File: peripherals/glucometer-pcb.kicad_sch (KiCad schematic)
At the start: 14 parts, among them U1 ESP32_DevKit_V1_DOIT

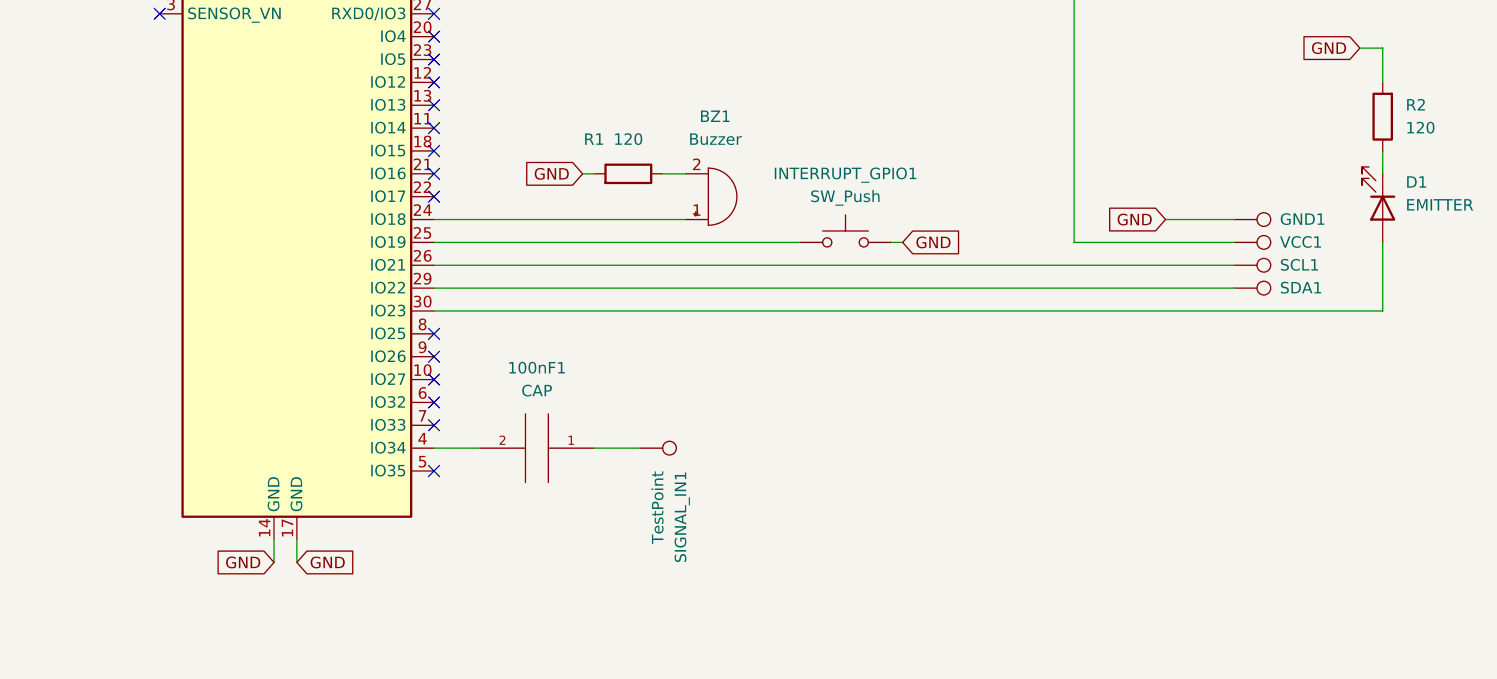
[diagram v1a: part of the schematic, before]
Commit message: updated pcb pads
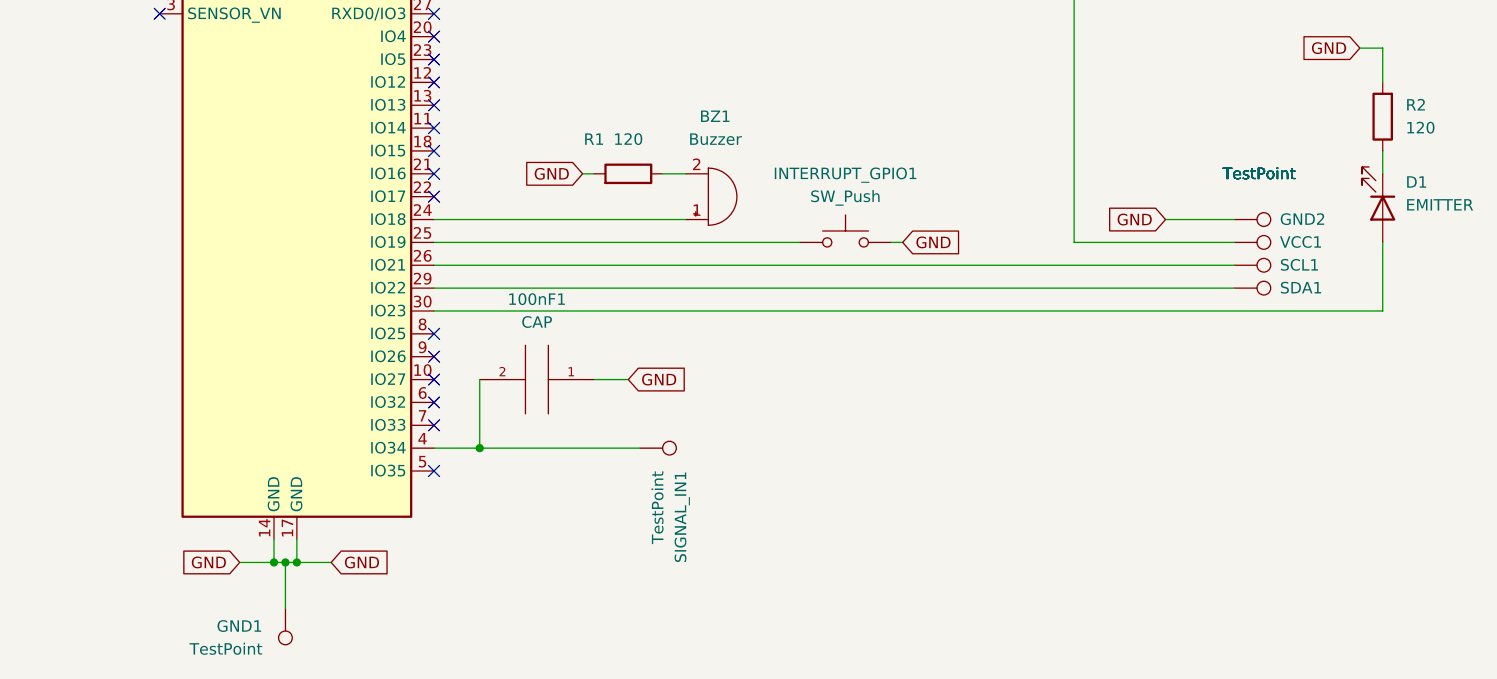
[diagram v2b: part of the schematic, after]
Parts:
- added GND1: TestPoint, TestPoint:TestPoint_Keystone_5015_Micro-Minature, symbol Connector:TestPoint
- GND2: renamed from GND1; value (none) -> TestPoint; footprint (none) -> TestPoint:TestPoint_Pad_2.0x2.0mm
- SCL1, SDA1, VCC1: value (none) -> TestPoint; footprint (none) -> TestPoint:TestPoint_Pad_2.0x2.0mm
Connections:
- net GND: now also 100nF1.1, GND1.1
- net at SIGNAL_IN1.1: now also 100nF1.2, U1.4 (IO34); no longer 100nF1.1
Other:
- moved on the sheet: 100nF1
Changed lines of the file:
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@@
 (kicad_sch (version 20211123) (generator eeschema)
   (paper "A4")
+  (junction (at 67.31 129.54) (diameter 0) (color 0 0 0 0)
+  )
+  (junction (at 66.04 129.54) (diameter 0) (color 0 0 0 0)
+  )
+  (junction (at 88.9 116.84) (diameter 0) (color 0 0 0 0)
+  )
   (junction (at 68.58 48.26) (diameter 0) (color 0 0 0 0)
+  )
+  (junction (at 68.58 129.54) (diameter 0) (color 0 0 0 0)
   )
   (no_connect (at 83.82 106.68))
@@
   (no_connect (at 83.82 114.3))
   (no_connect (at 83.82 86.36))
+  (wire (pts (xy 67.31 134.62) (xy 67.31 129.54))
+    (stroke (width 0) (type default) (color 0 0 0 0))
+  )
+  (wire (pts (xy 88.9 109.22) (xy 88.9 116.84))
+    (stroke (width 0) (type default) (color 0 0 0 0))
+  )
+  (wire (pts (xy 88.9 116.84) (xy 106.68 116.84))
+    (stroke (width 0) (type default) (color 0 0 0 0))
+  )
   (wire (pts (xy 83.82 101.6) (xy 189.23 101.6))
     (stroke (width 0) (type default) (color 0 0 0 0))
@@
     (stroke (width 0) (type default) (color 0 0 0 0))
   )
+  (wire (pts (xy 68.58 129.54) (xy 68.58 127))
+    (stroke (width 0) (type default) (color 0 0 0 0))
+  )
   (wire (pts (xy 83.82 99.06) (xy 172.72 99.06))
     (stroke (width 0) (type default) (color 0 0 0 0))
@@
     (stroke (width 0) (type default) (color 0 0 0 0))
   )
+  (wire (pts (xy 66.04 129.54) (xy 67.31 129.54))
+    (stroke (width 0) (type default) (color 0 0 0 0))
+  )
   (wire (pts (xy 154.94 93.98) (xy 154.94 48.26))
     (stroke (width 0) (type default) (color 0 0 0 0))
@@
     (stroke (width 0) (type default) (color 0 0 0 0))
   )
+  (wire (pts (xy 67.31 129.54) (xy 68.58 129.54))
+    (stroke (width 0) (type default) (color 0 0 0 0))
+  )
   (wire (pts (xy 83.82 91.44) (xy 111.76 91.44))
     (stroke (width 0) (type default) (color 0 0 0 0))
   )
-  (wire (pts (xy 101.6 116.84) (xy 106.68 116.84))
-    (stroke (width 0) (type default) (color 0 0 0 0))
-  )
   (wire (pts (xy 83.82 96.52) (xy 172.72 96.52))
     (stroke (width 0) (type default) (color 0 0 0 0))
@@
     (stroke (width 0) (type default) (color 0 0 0 0))
   )
+  (wire (pts (xy 66.04 129.54) (xy 66.04 127))
+    (stroke (width 0) (type default) (color 0 0 0 0))
+  )
+  (wire (pts (xy 101.6 109.22) (xy 105.41 109.22))
+    (stroke (width 0) (type default) (color 0 0 0 0))
+  )
+  (wire (pts (xy 83.82 116.84) (xy 88.9 116.84))
+    (stroke (width 0) (type default) (color 0 0 0 0))
+  )
   (wire (pts (xy 154.94 93.98) (xy 172.72 93.98))
     (stroke (width 0) (type default) (color 0 0 0 0))
   )
-  (wire (pts (xy 66.04 127) (xy 66.04 129.54))
+  (wire (pts (xy 66.04 129.54) (xy 62.23 129.54))
     (stroke (width 0) (type default) (color 0 0 0 0))
   )
@@
     (stroke (width 0) (type default) (color 0 0 0 0))
   )
-  (wire (pts (xy 83.82 116.84) (xy 88.9 116.84))
-    (stroke (width 0) (type default) (color 0 0 0 0))
-  )
   (wire (pts (xy 189.23 83.82) (xy 189.23 86.36))
     (stroke (width 0) (type default) (color 0 0 0 0))
@@
     (stroke (width 0) (type default) (color 0 0 0 0))
   )
-  (wire (pts (xy 68.58 127) (xy 68.58 129.54))
+  (wire (pts (xy 68.58 129.54) (xy 72.39 129.54))
     (stroke (width 0) (type default) (color 0 0 0 0))
   )
@@
     )
   )
-  (global_label "GND" (shape input) (at 68.58 129.54 0) (fields_autoplaced)
+  (global_label "GND" (shape input) (at 72.39 129.54 0) (fields_autoplaced)
     (effects (font (size 1.27 1.27)) (justify left))
-    (property "Referencias entre hojas" "${INTERSHEET_REFS}" (id 0) (at 74.8636 129.4606 0)
+    (property "Referencias entre hojas" "${INTERSHEET_REFS}" (id 0) (at 78.6736 129.4606 0)
       (effects (font (size 1.27 1.27)) (justify left) hide)
     )
@@
     )
   )
-  (global_label "GND" (shape input) (at 66.04 129.54 180) (fields_autoplaced)
+  (global_label "GND" (shape input) (at 62.23 129.54 180) (fields_autoplaced)
     (effects (font (size 1.27 1.27)) (justify right))
-    (property "Referencias entre hojas" "${INTERSHEET_REFS}" (id 0) (at 59.7564 129.4606 0)
+    (property "Referencias entre hojas" "${INTERSHEET_REFS}" (id 0) (at 55.9464 129.4606 0)
       (effects (font (size 1.27 1.27)) (justify right) hide)
     )
@@
     )
   )
+  (global_label "GND" (shape input) (at 105.41 109.22 0) (fields_autoplaced)
+    (effects (font (size 1.27 1.27)) (justify left))
+    (property "Referencias entre hojas" "${INTERSHEET_REFS}" (id 0) (at 111.6936 109.1406 0)
+      (effects (font (size 1.27 1.27)) (justify left) hide)
+    )
+  )
   (global_label "GND" (shape input) (at 135.89 93.98 0) (fields_autoplaced)
     (effects (font (size 1.27 1.27)) (justify left))
@@
     )
   )
+  (symbol (lib_id "Connector:TestPoint") (at 67.31 134.62 0) (mirror x) (unit 1)
+    (in_bom yes) (on_board yes) (fields_autoplaced)
+    (property "Reference" "GND1" (id 0) (at 64.77 136.6519 0)
+      (effects (font (size 1.27 1.27)) (justify right))
+    )
+    (property "Value" "TestPoint" (id 1) (at 64.77 139.1919 0)
+      (effects (font (size 1.27 1.27)) (justify right))
+    )
+    (property "Footprint" "TestPoint:TestPoint_Keystone_5015_Micro-Minature" (id 2) (at 72.39 134.62 0)
+      (effects (font (size 1.27 1.27)) hide)
+    )
+    (property "Datasheet" "~" (id 3) (at 72.39 134.62 0)
+      (effects (font (size 1.27 1.27)) hide)
+    )
+    (pin "1")
+  )
   (symbol (lib_id "Device:R") (at 105.41 86.36 270) (mirror x) (unit 1)
     (in_bom yes) (on_board yes)
@@
     (pin "1")
   )
-  (symbol (lib_id "pspice:CAP") (at 95.25 116.84 270) (unit 1)
-    (in_bom yes) (on_board yes) (fields_autoplaced)
-    (property "Reference" "100nF1" (id 0) (at 95.25 107.95 90))
-    (property "Value" "CAP" (id 1) (at 95.25 110.49 90))
-    (property "Footprint" "Capacitor_THT:C_Disc_D4.3mm_W1.9mm_P5.00mm" (id 2) (at 95.25 116.84 0)
-      (effects (font (size 1.27 1.27)) hide)
-    )
-    (property "Datasheet" "~" (id 3) (at 95.25 116.84 0)
+  (symbol (lib_id "pspice:CAP") (at 95.25 109.22 270) (unit 1)
+    (in_bom yes) (on_board yes) (fields_autoplaced)
+    (property "Reference" "100nF1" (id 0) (at 95.25 100.33 90))
+    (property "Value" "CAP" (id 1) (at 95.25 102.87 90))
+    (property "Footprint" "Capacitor_THT:C_Disc_D4.3mm_W1.9mm_P5.00mm" (id 2) (at 95.25 109.22 0)
+      (effects (font (size 1.27 1.27)) hide)
+    )
+    (property "Datasheet" "~" (id 3) (at 95.25 109.22 0)
       (effects (font (size 1.27 1.27)) hide)
     )
@@
   (symbol (lib_id "Connector:TestPoint") (at 172.72 91.44 270) (mirror x) (unit 1)
     (in_bom yes) (on_board yes)
-    (property "Reference" "GND1" (id 0) (at 177.8 91.44 90)
-      (effects (font (size 1.27 1.27)) (justify left))
-    )
-    (property "Value" "" (id 1) (at 171.45 86.36 90)
-      (effects (font (size 1.27 1.27)) (justify left))
-    )
-    (property "Footprint" "" (id 2) (at 172.72 86.36 0)
+    (property "Reference" "GND2" (id 0) (at 177.8 91.44 90)
+      (effects (font (size 1.27 1.27)) (justify left))
+    )
+    (property "Value" "TestPoint" (id 1) (at 171.45 86.36 90)
+      (effects (font (size 1.27 1.27)) (justify left))
+    )
+    (property "Footprint" "TestPoint:TestPoint_Pad_2.0x2.0mm" (id 2) (at 172.72 86.36 0)
       (effects (font (size 1.27 1.27)) hide)
     )
@@
       (effects (font (size 1.27 1.27)) (justify left))
     )
-    (property "Value" "" (id 1) (at 171.45 86.36 90)
-      (effects (font (size 1.27 1.27)) (justify left))
-    )
-    (property "Footprint" "" (id 2) (at 172.72 88.9 0)
+    (property "Value" "TestPoint" (id 1) (at 171.45 86.36 90)
+      (effects (font (size 1.27 1.27)) (justify left))
+    )
+    (property "Footprint" "TestPoint:TestPoint_Pad_2.0x2.0mm" (id 2) (at 172.72 88.9 0)
       (effects (font (size 1.27 1.27)) hide)
     )
@@
       (effects (font (size 1.27 1.27)) (justify left))
     )
-    (property "Value" "" (id 1) (at 171.45 86.36 90)
-      (effects (font (size 1.27 1.27)) (justify left))
-    )
-    (property "Footprint" "" (id 2) (at 172.72 93.98 0)
+    (property "Value" "TestPoint" (id 1) (at 171.45 86.36 90)
+      (effects (font (size 1.27 1.27)) (justify left))
+    )
+    (property "Footprint" "TestPoint:TestPoint_Pad_2.0x2.0mm" (id 2) (at 172.72 93.98 0)
       (effects (font (size 1.27 1.27)) hide)
     )
@@
       (effects (font (size 1.27 1.27)) (justify left))
     )
-    (property "Value" "" (id 1) (at 171.45 86.36 90)
-      (effects (font (size 1.27 1.27)) (justify left))
-    )
-    (property "Footprint" "" (id 2) (at 172.72 91.44 0)
+    (property "Value" "TestPoint" (id 1) (at 171.45 86.36 90)
+      (effects (font (size 1.27 1.27)) (justify left))
+    )
+    (property "Footprint" "TestPoint:TestPoint_Pad_2.0x2.0mm" (id 2) (at 172.72 91.44 0)
       (effects (font (size 1.27 1.27)) hide)
     )
@@
       (reference "D1") (unit 1) (value "EMITTER") (footprint "LED_THT:LED_D3.0mm_Clear")
     )
+    (path "/1748450e-a8ca-4e49-95b9-4d9e086df7db"
+      (reference "GND1") (unit 1) (value "TestPoint") (footprint "TestPoint:TestPoint_Keystone_5015_Micro-Minature")
+    )
     (path "/316369ce-281e-4fab-8ad5-3b8ffc87cc69"
-      (reference "GND1") (unit 1) (value "TestPoint") (footprint "TestPoint:TestPoint_Pad_2.0x2.0mm")
+      (reference "GND2") (unit 1) (value "TestPoint") (footprint "TestPoint:TestPoint_Pad_2.0x2.0mm")
     )
     (path "/aa939002-c65a-4bc5-8b33-1d5bc4c91f9d"

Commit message: updated PCBs
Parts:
- added R2: 27K, Resistor_THT:R_Axial_DIN0204_L3.6mm_D1.6mm_P7.62mm_Horizontal, symbol Device:R
- added R3: 100K, Resistor_THT:R_Axial_DIN0204_L3.6mm_D1.6mm_P7.62mm_Horizontal, symbol Device:R
- renumbered R2 to R4, SDA1 to SCL1, SCL1 to SDA1
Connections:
- net GND: now also R3.2
- net VIN: now reaches BATTERY1.1 (+), U1.15 (VIN)
- net VIN: now also R2.2
- net at U1.7 (IO33): now also R2.1, R3.1
- no-connect marks 20 -> 19
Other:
- moved on the sheet: 100nF1, BATTERY1

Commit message: small changes and (temp V divisor)
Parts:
- added R2, R3: 100K, Resistor_THT:R_Axial_DIN0204_L3.6mm_D1.6mm_P7.62mm_Horizontal, symbol Device:R
- R2: value 27K -> (none)
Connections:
- net GND: now also R3.2
- net VIN: now also R2.2
- new net ADC_IN: R2.1, R3.1
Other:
- moved on the sheet: 3V3_OUT1, BATTERY1, BZ1, D1, GND2, R1, R2, R3, R4, SCL1, SDA1, VCC1
